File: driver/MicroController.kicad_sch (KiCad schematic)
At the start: 1 part

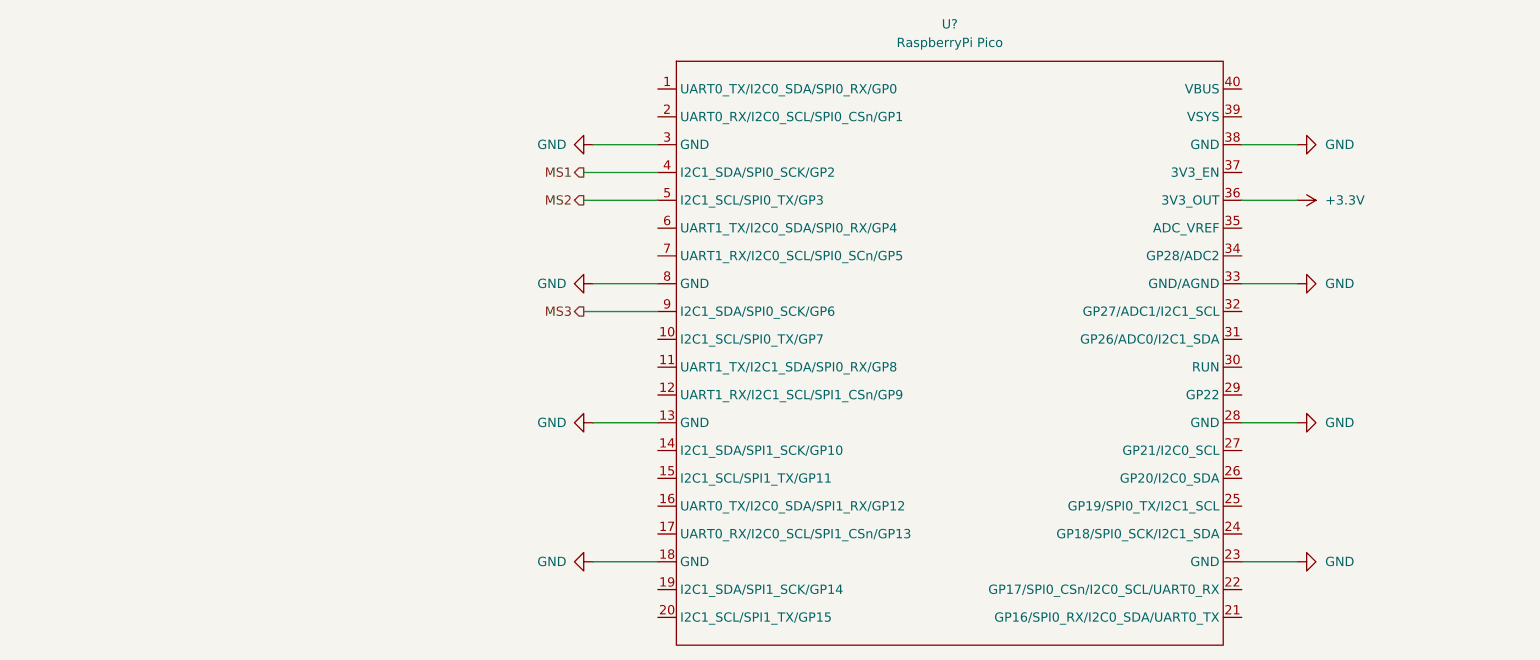
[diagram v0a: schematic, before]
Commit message: 部品配置完了
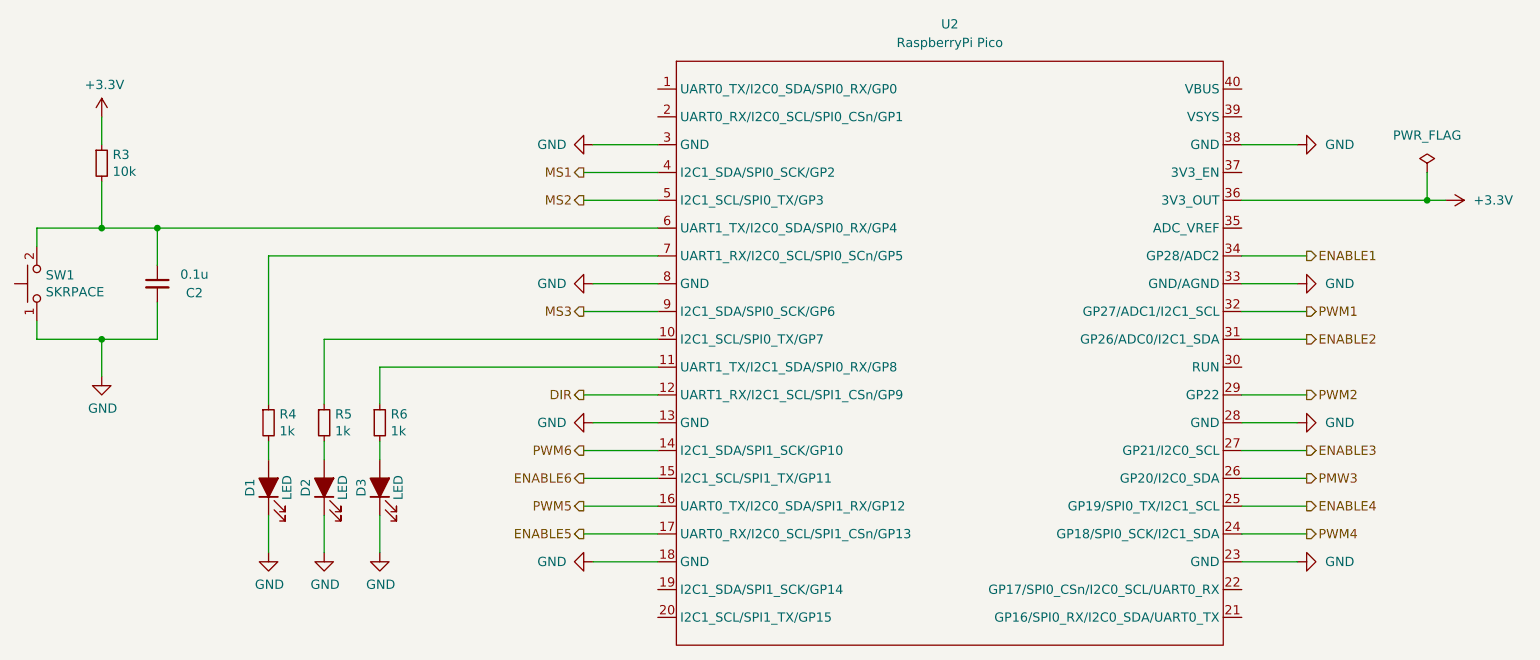
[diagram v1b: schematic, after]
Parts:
- added C2: 0.1u, Capacitor_SMD:C_0603_1608Metric_Pad1.08x0.95mm_HandSolder, symbol Device:C_Small
- added D1, D2, D3: LED, LED_SMD:LED_0603_1608Metric_Pad1.05x0.95mm_HandSolder, symbol Device:LED_ALT
- added R3: 10k, Resistor_SMD:R_0603_1608Metric_Pad0.98x0.95mm_HandSolder, symbol Device:R_Small
- added R4, R5, R6: 1k, Resistor_SMD:R_0805_2012Metric_Pad1.20x1.40mm_HandSolder, symbol Device:R_Small
- added SW1: SKRPACE, Button_Switch_SMD:SW_Push_1P1T_NO_Vertical_Wuerth_434133025816, symbol My_Device:SKRPACE
- U2: renamed from U?; footprint (none) -> stepper_music_lib:raspberrypi_pico
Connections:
- net +3.3V: now also R3.1
- net GND: now also C2.2, D1.1 (K), D2.1 (K), D3.1 (K), SW1.1
- net at U2.10 (I2C1_SCL/SPI0_TX/GP7): now also R5.1
- net at U2.11 (UART1_TX/I2C1_SDA/SPI0_RX/GP8): now also R6.1
- net DIR: now reaches U2.12 (UART1_RX/I2C1_SCL/SPI1_CSn/GP9)
- net PWM6: now reaches U2.14 (I2C1_SDA/SPI1_SCK/GP10)
- net ENABLE6: now reaches U2.15 (I2C1_SCL/SPI1_TX/GP11)
- net PWM5: now reaches U2.16 (UART0_TX/I2C0_SDA/SPI1_RX/GP12)
- net ENABLE5: now reaches U2.17 (UART0_RX/I2C0_SCL/SPI1_CSn/GP13)
- net PWM4: now reaches U2.24 (GP18/SPI0_SCK/I2C1_SDA)
- net ENABLE4: now reaches U2.25 (GP19/SPI0_TX/I2C1_SCL)
- net PMW3: now reaches U2.26 (GP20/I2C0_SDA)
- net ENABLE3: now reaches U2.27 (GP21/I2C0_SCL)
- net PWM2: now reaches U2.29 (GP22)
- net ENABLE2: now reaches U2.31 (GP26/ADC0/I2C1_SDA)
- net PWM1: now reaches U2.32 (GP27/ADC1/I2C1_SCL)
- net ENABLE1: now reaches U2.34 (GP28/ADC2)
- net at U2.6 (UART1_TX/I2C0_SDA/SPI0_RX/GP4): now also C2.1, R3.2, SW1.2
- net at U2.7 (UART1_RX/I2C0_SCL/SPI0_SCn/GP5): now also R4.1
- new net: D2.2 (A), R5.2
- new net: D3.2 (A), R6.2
- new net: D1.2 (A), R4.2
